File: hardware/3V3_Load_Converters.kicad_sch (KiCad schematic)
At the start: 74 parts, among them J23 61300311121, J24 61300311121, Q26 SI2302DDS-T1-GE3, Q27 SI2302DDS-T1-GE3, Q28 EPC2016C, Q29 EPC2016C, Q30 EPC2016C, Q31 EPC2016C, U30 LTC3833EUDC-TRPBF, U31 LTC3833EUDC-TRPBF, U4 INA199C1DCKR

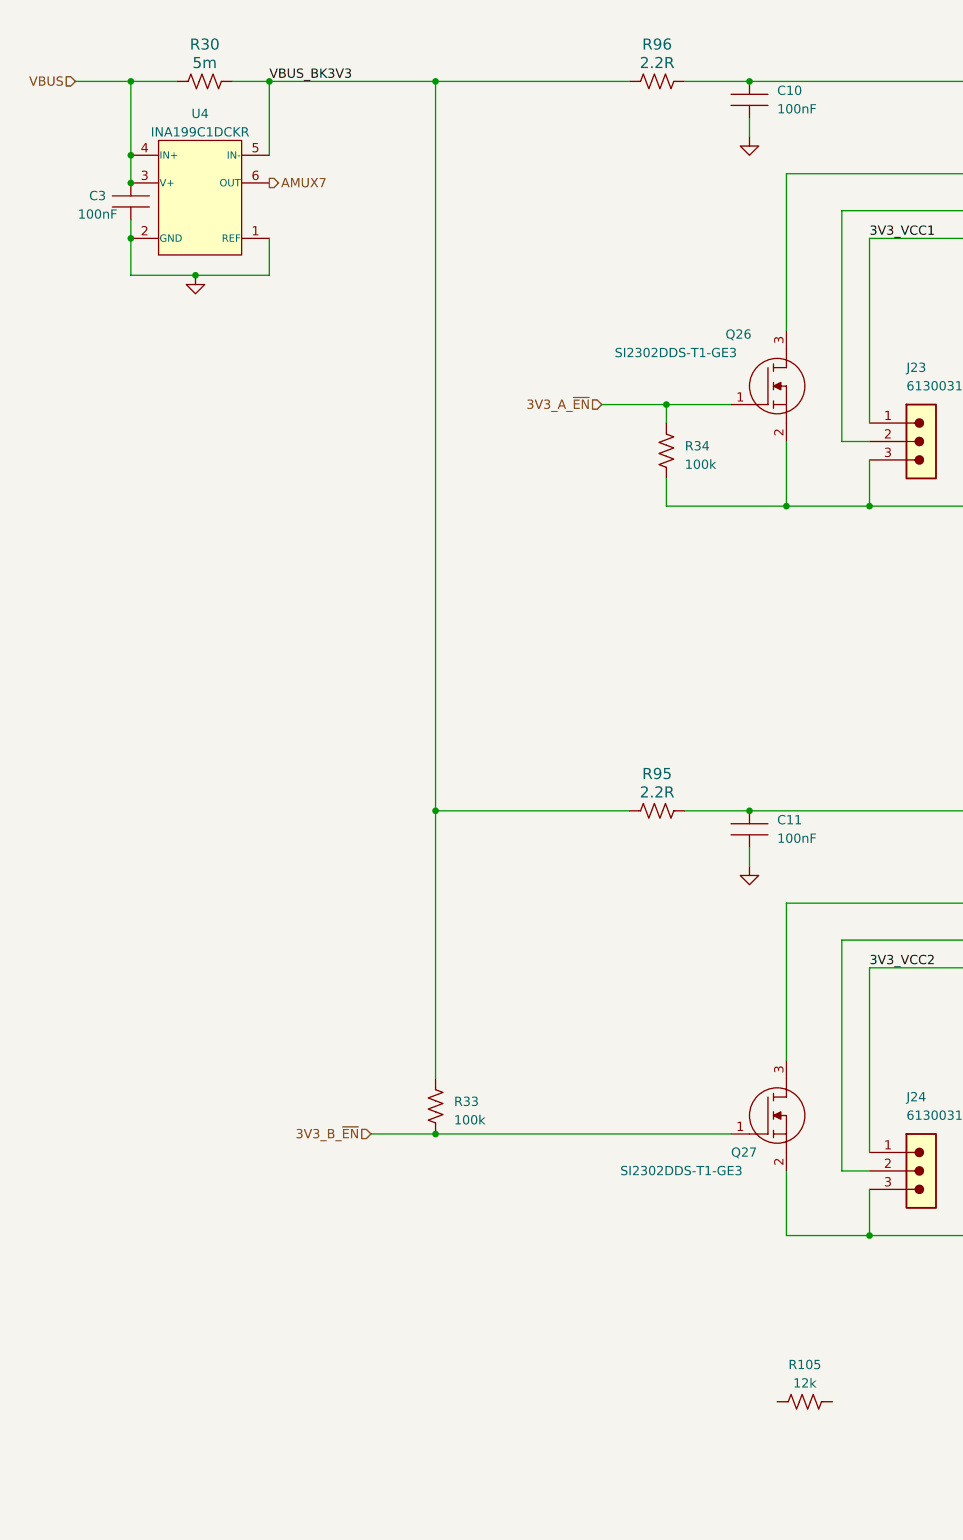
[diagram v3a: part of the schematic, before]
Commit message: hardware: Updating some footprints and 3D models.
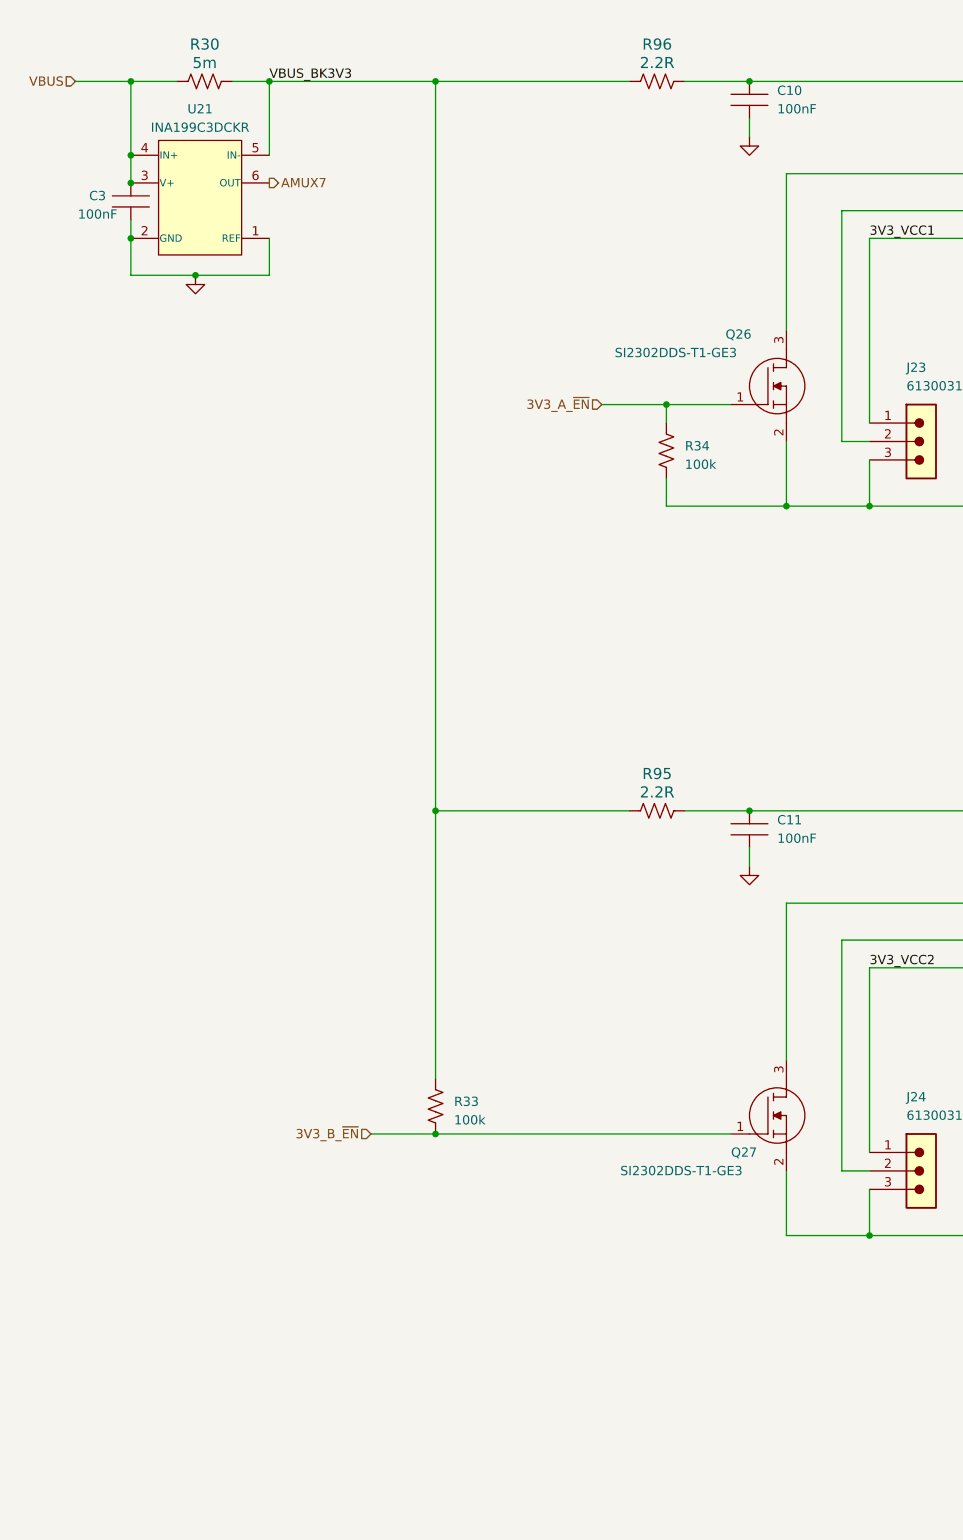
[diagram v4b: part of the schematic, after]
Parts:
- removed R105: 12k, footprints:CRCW060312K0FKEAHP, symbol CRCW060312K0FKEAHP:CRCW060312K0FKEAHP
- removed U4: INA199C1DCKR, footprints:INA199C1DCKR, symbol INA199C1DCKR:INA199xxDCK
- added U21: INA199C3DCKR, Package_TO_SOT_SMD:SOT-363_SC-70-6, symbol INA199C3DCKR:INA199xxDCK
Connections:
- net AMUX7: now also U21.6 (OUT)
- net GND: now also U21.1 (REF), U21.2 (GND)
- net VBUS: now also U21.3 (V+), U21.4 (IN+)
- net VBUS_BK3V3: now also U21.5 (IN-)
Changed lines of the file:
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@@
   (junction (at 74.93 125.73) (diameter 0) (color 0 0 0 0)
   )
+  (junction (at 33.02 46.99) (diameter 0) (color 0 0 0 0)
+  )
   (junction (at 325.12 121.92) (diameter 0) (color 0 0 0 0)
   )
@@
   (junction (at 256.54 24.13) (diameter 0) (color 0 0 0 0)
   )
+  (junction (at 33.02 35.56) (diameter 0) (color 0 0 0 0)
+  )
   (junction (at 256.54 124.46) (diameter 0) (color 0 0 0 0)
   )
@@
   (junction (at 256.54 135.89) (diameter 0) (color 0 0 0 0)
   )
-  (junction (at 33.02 39.37) (diameter 0) (color 0 0 0 0)
-  )
   (junction (at 173.99 83.82) (diameter 0) (color 0 0 0 0)
   )
@@
   (junction (at 347.98 48.26) (diameter 0) (color 0 0 0 0)
   )
-  (junction (at 33.02 46.99) (diameter 0) (color 0 0 0 0)
-  )
   (junction (at 335.28 121.92) (diameter 0) (color 0 0 0 0)
   )
@@
   (junction (at 256.54 48.26) (diameter 0) (color 0 0 0 0)
   )
+  (junction (at 33.02 39.37) (diameter 0) (color 0 0 0 0)
+  )
   (junction (at 194.31 83.82) (diameter 0) (color 0 0 0 0)
   )
@@
   (junction (at 74.93 25.4) (diameter 0) (color 0 0 0 0)
   )
-  (junction (at 33.02 35.56) (diameter 0) (color 0 0 0 0)
-  )
   (wire (pts (xy 372.11 175.26) (xy 372.11 195.58))
     (stroke (width 0) (type default))
@@
     (stroke (width 0) (type default))
   )
-  (wire (pts (xy 33.02 25.4) (xy 33.02 35.56))
-    (stroke (width 0) (type default))
-  )
   (wire (pts (xy 290.83 30.48) (xy 290.83 21.59))
     (stroke (width 0) (type default))
   )
-  (wire (pts (xy 33.02 35.56) (xy 33.02 39.37))
+  (wire (pts (xy 33.02 25.4) (xy 33.02 35.56))
     (stroke (width 0) (type default))
   )
@@
     (stroke (width 0) (type default))
   )
-  (wire (pts (xy 33.02 52.07) (xy 33.02 46.99))
-    (stroke (width 0) (type default))
-  )
   (wire (pts (xy 347.98 172.72) (xy 347.98 173.99))
     (stroke (width 0) (type default))
@@
     (stroke (width 0) (type default))
   )
+  (wire (pts (xy 33.02 35.56) (xy 33.02 39.37))
+    (stroke (width 0) (type default))
+  )
   (wire (pts (xy 354.33 127) (xy 354.33 129.54))
     (stroke (width 0) (type default))
@@
     (stroke (width 0) (type default))
   )
+  (wire (pts (xy 33.02 46.99) (xy 33.02 52.07))
+    (stroke (width 0) (type default))
+  )
   (wire (pts (xy 359.41 48.26) (xy 359.41 52.07))
     (stroke (width 0) (type default))
@@
     )
   )
+  (symbol (lib_id "INA199C3DCKR:INA199xxDCK") (at 20.32 54.61 0) (unit 1)
+    (in_bom yes) (on_board yes) (dnp no) (fields_autoplaced)
+    (property "Reference" "U21" (at 42.545 29.21 0)
+      (effects (font (size 1.27 1.27)))
+    )
+    (property "Value" "INA199C3DCKR" (at 42.545 31.75 0)
+      (effects (font (size 1.27 1.27)))
+    )
+    (property "Footprint" "Package_TO_SOT_SMD:SOT-363_SC-70-6" (at 43.942 53.848 0)
+      (effects (font (size 1.27 1.27)) hide)
+    )
+    (property "Datasheet" "http://www.ti.com/lit/ds/symlink/ina199.pdf" (at 42.926 56.134 0)
+      (effects (font (size 1.27 1.27)) hide)
+    )
+    (pin "1")
+    (pin "2")
+    (pin "3")
+    (pin "4")
+    (pin "5")
+    (pin "6")
+    (instances
+      (project "eps-re_project"
+        (path "/2eebaa11-d7ed-4bfd-bc8e-988f68654d29/6f34948c-43a8-4614-b8ed-90c5b6b9b243"
+          (reference "U21") (unit 1)
+        )
+      )
+    )
+  )
   (symbol (lib_id "C0603C220K5RACAUTO:C0603C220K5RACAUTO") (at 359.41 52.07 0) (unit 1)
     (in_bom yes) (on_board yes) (dnp no)
@@
     )
   )
-  (symbol (lib_id "INA199C1DCKR:INA199xxDCK") (at 20.32 54.61 0) (unit 1)
-    (in_bom yes) (on_board yes) (dnp no)
-    (property "Reference" "U4" (at 42.545 29.845 0)
-      (effects (font (size 1.27 1.27)))
-    )
-    (property "Value" "INA199C1DCKR" (at 42.545 32.385 0)
-      (effects (font (size 1.27 1.27)))
-    )
-    (property "Footprint" "footprints:INA199C1DCKR " (at 43.942 53.848 0)
-      (effects (font (size 1.27 1.27)) hide)
-    )
-    (property "Datasheet" "http://www.ti.com/lit/ds/symlink/ina199.pdf" (at 42.926 56.134 0)
-      (effects (font (size 1.27 1.27)) hide)
-    )
-    (pin "1")
-    (pin "2")
-    (pin "3")
-    (pin "4")
-    (pin "5")
-    (pin "6")
-    (instances
-      (project "eps-re_project"
-        (path "/2eebaa11-d7ed-4bfd-bc8e-988f68654d29/b2d6a676-b7d9-423e-8a54-05279452700b"
-          (reference "U4") (unit 1)
-        )
-        (path "/2eebaa11-d7ed-4bfd-bc8e-988f68654d29/4f028e55-4c46-47b6-9c45-f6b50d9d4db8"
-          (reference "U14") (unit 1)
-        )
-        (path "/2eebaa11-d7ed-4bfd-bc8e-988f68654d29/6cd5fe02-9b19-49bf-9109-b0a2c2f10c14"
-          (reference "U22") (unit 1)
-        )
-        (path "/2eebaa11-d7ed-4bfd-bc8e-988f68654d29/6f34948c-43a8-4614-b8ed-90c5b6b9b243"
-          (reference "U21") (unit 1)
-        )
-      )
-      (project "EPS Analogico"
-        (path "/9af6272d-3cb8-4e37-b792-5888e300588f"
-          (reference "U1") (unit 1)
-        )
-      )
-    )
-  )
   (symbol (lib_id "power:GND") (at 372.11 195.58 0) (unit 1)
     (in_bom yes) (on_board yes) (dnp no) (fields_autoplaced)
@@
         )
       )
-    )
-  )
-  (symbol (lib_id "CRCW060312K0FKEAHP:CRCW060312K0FKEAHP") (at 119.38 207.01 0) (unit 1)
-    (in_bom yes) (on_board yes) (dnp no) (fields_autoplaced)
-    (property "Reference" "R105" (at 125.73 201.93 0)
-      (effects (font (size 1.27 1.27)))
-    )
-    (property "Value" "12k" (at 125.73 204.47 0)
-      (effects (font (size 1.27 1.27)))
-    )
-    (property "Footprint" "footprints:CRCW060312K0FKEAHP" (at 119.38 196.85 0)
-      (effects (font (size 1.27 1.27)) (justify left) hide)
-    )
-    (property "Datasheet" "http://www.vishay.com/docs/20043/crcwhpe3.pdf" (at 119.38 194.31 0)
-      (effects (font (size 1.27 1.27)) (justify left) hide)
-    )
-    (property "automotive" "Yes" (at 119.38 191.77 0)
-      (effects (font (size 1.27 1.27)) (justify left) hide)
-    )
-    (property "automotive grade" "Grade 0" (at 119.38 189.23 0)
-      (effects (font (size 1.27 1.27)) (justify left) hide)
-    )
-    (property "category" "Res" (at 119.38 186.69 0)
-      (effects (font (size 1.27 1.27)) (justify left) hide)
-    )
-    (property "composition" "Thick Film" (at 119.38 184.15 0)
-      (effects (font (size 1.27 1.27)) (justify left) hide)
-    )
-    (property "device class L1" "Passive Components" (at 119.38 181.61 0)
-      (effects (font (size 1.27 1.27)) (justify left) hide)
-    )
-    (property "device class L2" "Resistors" (at 119.38 179.07 0)
-      (effects (font (size 1.27 1.27)) (justify left) hide)
-    )
-    (property "device class L3" "Chip SMD Resistors" (at 119.38 176.53 0)
-      (effects (font (size 1.27 1.27)) (justify left) hide)
-    )
-    (property "digikey description" "" (at 119.38 173.99 0)
-      (effects (font (size 1.27 1.27)) (justify left) hide)
-    )
-    (property "digikey part number" "" (at 119.38 171.45 0)
-      (effects (font (size 1.27 1.27)) (justify left) hide)
-    )
-    (property "height" "0.55mm" (at 119.38 168.91 0)
-      (effects (font (size 1.27 1.27)) (justify left) hide)
-    )
-    (property "ipc land pattern name" "RESC16085X45" (at 119.38 166.37 0)
-      (effects (font (size 1.27 1.27)) (justify left) hide)
-    )
-    (property "lead free" "Yes" (at 119.38 163.83 0)
-      (effects (font (size 1.27 1.27)) (justify left) hide)
-    )
-    (property "library id" "e050c09dfdbc8558" (at 119.38 161.29 0)
-      (effects (font (size 1.27 1.27)) (justify left) hide)
-    )
-    (property "manufacturer" "Vishay" (at 119.38 158.75 0)
-      (effects (font (size 1.27 1.27)) (justify left) hide)
-    )
-    (property "mouser description" "" (at 119.38 156.21 0)
-      (effects (font (size 1.27 1.27)) (justify left) hide)
-    )
-    (property "mouser part number" "" (at 119.38 153.67 0)
-      (effects (font (size 1.27 1.27)) (justify left) hide)
-    )
-    (property "package" "0603" (at 119.38 151.13 0)
-      (effects (font (size 1.27 1.27)) (justify left) hide)
-    )
-    (property "power" "250mW" (at 119.38 148.59 0)
-      (effects (font (size 1.27 1.27)) (justify left) hide)
-    )
-    (property "power rating" "0.33W" (at 119.38 146.05 0)
-      (effects (font (size 1.27 1.27)) (justify left) hide)
-    )
-    (property "resistance" "12kΩ" (at 119.38 143.51 0)
-      (effects (font (size 1.27 1.27)) (justify left) hide)
-    )
-    (property "rohs" "Yes" (at 119.38 140.97 0)
-      (effects (font (size 1.27 1.27)) (justify left) hide)
-    )
-    (property "series" "CRCW-HP e3" (at 119.38 138.43 0)
-      (effects (font (size 1.27 1.27)) (justify left) hide)
-    )
-    (property "temperature coefficient" "100ppm/°C" (at 119.38 135.89 0)
-      (effects (font (size 1.27 1.27)) (justify left) hide)
-    )
-    (property "temperature range high" "+155°C" (at 119.38 133.35 0)
-      (effects (font (size 1.27 1.27)) (justify left) hide)
-    )
-    (property "temperature range low" "-55°C" (at 119.38 130.81 0)
-      (effects (font (size 1.27 1.27)) (justify left) hide)
-    )
-    (property "tolerance" "1%" (at 119.38 128.27 0)
-      (effects (font (size 1.27 1.27)) (justify left) hide)
-    )
-    (property "voltage rating" "75V" (at 119.38 125.73 0)
-      (effects (font (size 1.27 1.27)) (justify left) hide)
-    )
-    (pin "1")
-    (pin "2")
-    (instances
-      (project "eps-re_project"
-        (path "/2eebaa11-d7ed-4bfd-bc8e-988f68654d29/6f34948c-43a8-4614-b8ed-90c5b6b9b243"
-          (reference "R105") (unit 1)
-        )
-      )
